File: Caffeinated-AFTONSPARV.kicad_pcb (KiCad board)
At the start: 4 copper layers, 42.5 x 16.1 mm, 38 parts, among them J1 PWR, J2 LED, J3 TagConnect, J4 USB, Q1 AO3400A, Q2 AO3400A, Q3 AO3400A, SW1 SW_Push, U1 ESP32-C3-MINI-1-[H/N]4, U2 SY8201ABC

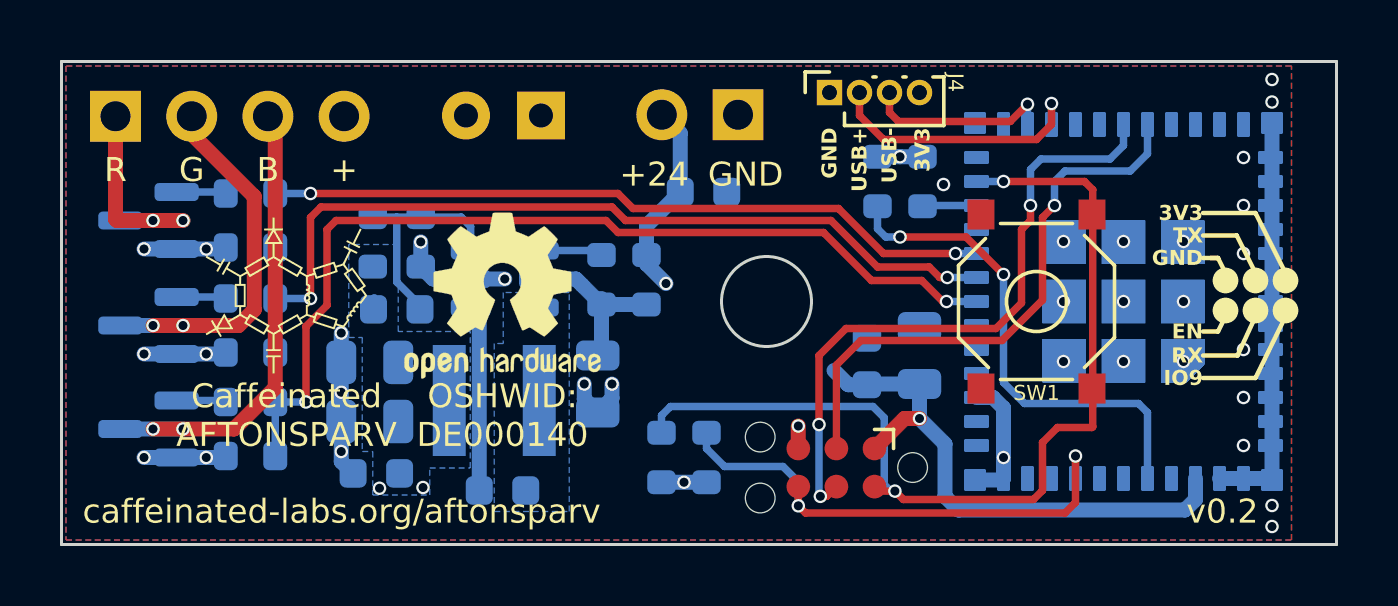
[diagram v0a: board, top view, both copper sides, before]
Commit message: feat(): Update silkscreen, ibom, use smaller sw
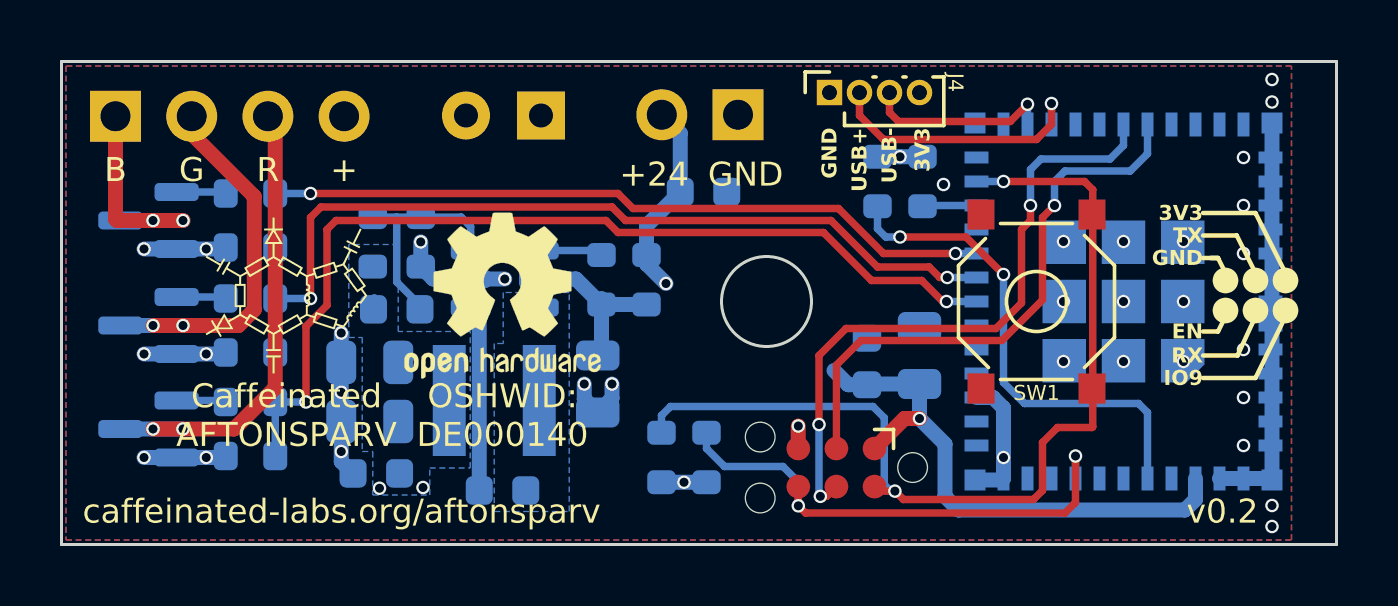
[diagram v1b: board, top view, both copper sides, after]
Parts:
- removed the U1 at (167.9, 100.0)
